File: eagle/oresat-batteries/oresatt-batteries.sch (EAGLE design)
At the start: 22 parts, among them U1 TCAN330

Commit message: Finished first draft of schematics.
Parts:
- removed Y1: (no value), low-gain-radio:CRYSTAL2.5X2.0MM
- added C10, C11, C12, C13: 100n, rcl:C-EUC0603
- added C8, C9: 20p, rcl:C-EUC0603
- added CF2: 2MM-RA-1X8, oresat-batteries:2MM-RA-1X8
- added D2: BAS40, diode:BAS40
- added R10, R12: 10k, rcl:R-US_R0603
- added R11, R7: (no value), rcl:R-US_R0603
- added R13: DNP/0, rcl:R-US_R0603
- added R8, R9: 4.7k, rcl:R-US_R0603
- added U$10, U$11, U$15, U$6, U$7, U$9: TP, oresat-batteries:TP
- added U2: STM32F042K6, oresat-batteries:STM32F042K6
- added X1: 16MHz, low-gain-radio:CRYSTAL-WITH-GND
- R1: value Sense -> THERMISTER
- R3: value Sense -> .01-.05
- R4: value Sense -> 200k .1%
- U$4: value STM32F042G -> TP; device oresat-batteries:STM32F042G -> oresat-batteries:TP
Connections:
- net N$1 renamed ADP_THR
- net N$10 renamed BQVMIN
- net N$2 renamed LEDNP
- net N$3 renamed ADP_LED
- net N$9 renamed STC_VIN
- removed net N$5: C5.1, CF1.3, U$1.VIN
- removed net N$6: C4.1
- removed net N$8: R3.2
- new net ADP_CBP: C4.1, U$1.CBP
- new net BQBAT: C1.1, R7.1, U$2.BAT
- new net CAN_EN: U1.SHDN, U2.PA10
- new net CAN_LSTN: U1.S, U2.PA9
- new net CAN_RX: U1.RXD, U2.PA11
- new net CAN_TX: U1.TXD, U2.PA12
- new net ISO_S: C3.1, CF1.2, U$1.ISO_S
- new net N$1: C7.2, R11.1, U$5.VCC
- new net N$2: R12.2, U2.PB8-BOOT0
- new net N$3: R10.1, R13.2, U$5.IO0
- new net N$31: CF2.3, U2.NRST
- new net OSC_IN: C8.1, U2.PF0-OSC_IN, X1.1
- new net OSC_OUT: C9.1, U2.PF1-OSC_OUT, X1.2
- new net SCL: R8.1, U$1.SCL, U$5.SCL, U2.PB6
- new net SDA: R9.1, U$1.SDA, U$5.SDA, U2.PB7
- new net STC_CG: R3.2, U$5.CG
- new net STC_IO: R13.1, U2.PB5
- new net STM_DEBUG: CF2.8, U2.PA4
- new net SWCLK: CF2.4, U2.PA14-SWCLK
- new net SWDIO: CF2.5, U2.PA13-SWDIO
- new net USART2_RX: CF2.7, U2.PA3
- new net USART2_TX: CF2.6, U2.PA2
- new net VSOLAR: C5.1, CF1.3, R8.2, R9.2, U$1.VIN
- net GND: now also C10.2, C11.2, C12.2, C13.2, C8.2, C9.2, CF2.1, R12.1, U1.GND, U2.VSS, X1.SHIELD
- net N$4: now also D2.C; no longer C3.1, U$1.ISO_S
- net VBAT+: now also C10.1, C11.1, C12.1, C13.1, CF2.2, D2.A, R11.2, R7.2, U1.VCC, U2.VDD, U2.VDDA, U2.VDDIO2; no longer C1.1, C7.2, U$2.BAT, U$5.VCC
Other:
- note added: "CAN_EN"
- note added: "CAN_LSTN"
- note added: "CAN_RX"
- note added: "CAN_TX"
- note added: "DEBUG"
- note added: "DO I WANT TO SHUTDOWN?"
- note added: "MISSING: Resistive heater Full SHUTDOWN"
- note added: "RESET"
- note added: "SCL"
- note added: "SDA"
- note added: "SWCLK"
- note added: "SWDIO"
- note added: "USART2_RX"
- note added: "USART2_TX"
- note added: "VBATT+"
- note added: "VSOLAR"
- note added: "WE NEED A PLACE TO CHAT"
- note added: "WE NEED FETS! 20 AMPS MAX DISCHARGE"
- moved on the sheet: C1, C2, C3, C4, C5, C6, C7, CF1, LED1, R1, R2, R3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

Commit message: Minor clean up, added debug board, serial marker
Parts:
- added DEBUG_DNP: (no value), pinhead:PINHD-2X8
- added U$12, U$16, U$17, U$8: TP, oresat-batteries:TP
- added U$13, U$14: CSD16340Q3, oresat-batteries:CSD16340Q3
- R8, R9: value 4.7k -> 1.6k
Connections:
- removed net VBAT+: C10.1, C11.1, C12.1, C13.1, C2.1, CF2.2, D2.A, R11.2, R5.1, R7.2, U$1.BAT_SNS, U$1.ISO_B, U1.VCC, U2.VDD, U2.VDDA, U2.VDDIO2
- new net N$10: U$14.G, U$2.DOUT
- new net N$11: U$13.G, U$2.COUT
- new net N$5: CF1.4, DEBUG_DNP.13, DEBUG_DNP.14, U1.CANH
- new net N$6: CF1.5, DEBUG_DNP.11, DEBUG_DNP.12, U1.CANL
- new net N$9: U$13.D, U$14.D
- new net VBATT+: C10.1, C11.1, C12.1, C13.1, C2.1, CF2.2, D2.A, DEBUG_DNP.1, DEBUG_DNP.2, R11.2, R5.1, R7.2, R8.2, R9.2, U$1.BAT_SNS, U$1.ISO_B, U1.VCC, U2.VDD, U2.VDDA, U2.VDDIO2
- net GND: now also DEBUG_DNP.15, DEBUG_DNP.16, U$13.S
- net SCL: now also R9.1; no longer R8.1
- net SDA: now also R8.1; no longer R9.1
- net STC_CG: now also U$14.S
- net USART2_RX: now also DEBUG_DNP.5, DEBUG_DNP.6
- net USART2_TX: now also DEBUG_DNP.3, DEBUG_DNP.4
- net VSOLAR: now also DEBUG_DNP.7, DEBUG_DNP.8; no longer R8.2, R9.2
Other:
- note added: "CANH"
- note added: "CANL"
- note added: "GND"
- note added: "High Side Battery shut-off"
- note added: "Low side shut-off NANOracks req"
- note added: "MISSING: Resistive heater Full SHUTDOWN Two high one low complete crowbar"
- note added: "UARTRX"
- note added: "UARTX"
- note added: "add ground pin clips NP"
- note added: "add pins"
- note removed: "MISSING: Resistive heater Full SHUTDOWN"
- note removed: "WE NEED A PLACE TO CHAT"
- note removed: "WE NEED FETS! 20 AMPS MAX DISCHARGE"
- moved on the sheet: C1, C2, C3, C4, C5, CF1, D2, LED1, R1, R2, R5, R6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

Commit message: Added, resistive heater, half of shutdown circuitry, connected DIG_IOx and SYS_EN pins.
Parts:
- added R14: 100k, rcl:R-US_R0603
- added U$18, U$19, U$20: CSD16340Q3, oresat-batteries:CSD16340Q3
- added U$21: 4.19, oresat-batteries:RES_HEATER
- U$3: value 1.5AHBATT -> 2AHBATT; device oresat-batteries:1.5AHBATT -> oresat-batteries:2AHBATT
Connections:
- net N$11 renamed COUT
- net N$9 renamed BETSHUT
- new net BATTHICUT: U$19.D, U$3.V+
- new net BQKILL: R6.2, U$18.D, U$2.VSS
- new net DOUT: CF1.40, R14.1, U$14.G, U$18.G, U$19.G, U$2.DOUT
- new net N$11: U$1.DIG_IO3, U2.PB4
- new net N$13: U$20.S, U$21.1
- new net N$14: U$20.G, U2.PA1
- new net N$8: U$1.SYS_EN, U2.PB0
- new net N$9: U$1.DIG_IO1, U2.PB1
- net GND: now also U$18.S, U$21.2; no longer R6.2, U$2.VSS
- net N$10: now also U$1.DIG_IO2, U2.PB3; no longer U$14.G, U$2.DOUT
- net STC_CG: now also U$3.V-
- net STC_VIN: now also R5.1; no longer R5.2
- net VBATT+: now also R14.2, R5.2, U$19.S, U$20.D; no longer R5.1
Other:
- note added: "DIG_IO1"
- note added: "DIG_IO2"
- note added: "DIG_IO3"
- note added: "HEAT"
- note added: "SHORT_BAR"
- note added: "SYS_EN"
- note added: "This won't work"
- note added: "VBATTSUPP"
- note removed: "High Side Battery shut-off"
- note removed: "Low side shut-off NANOracks req"
- moved on the sheet: C1, C10, C11, C12, C13, C2, C4, C6, CF2, DEBUG_DNP, R12, R5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

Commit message: Fixed Shutdown Circuit, Added more ground pins, cleaned up schematic
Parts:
- added R15: 100k, rcl:R-US_R0603
- added U$22, U$23: TP, oresat-batteries:TP
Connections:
- new net SHORTBAR: CF1.40, R14.1, R15.1, U$18.G, U$19.G
- net DOUT: no longer CF1.40, R14.1, U$18.G, U$19.G
- net GND: now also R15.2
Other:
- note added: "ISO_Sx"
- note removed: "DO I WANT TO SHUTDOWN?"
- note removed: "MISSING: Resistive heater Full SHUTDOWN Two high one low complete crowbar"
- note removed: "This won't work"
- moved on the sheet: D2, U$16, U$17, U$18

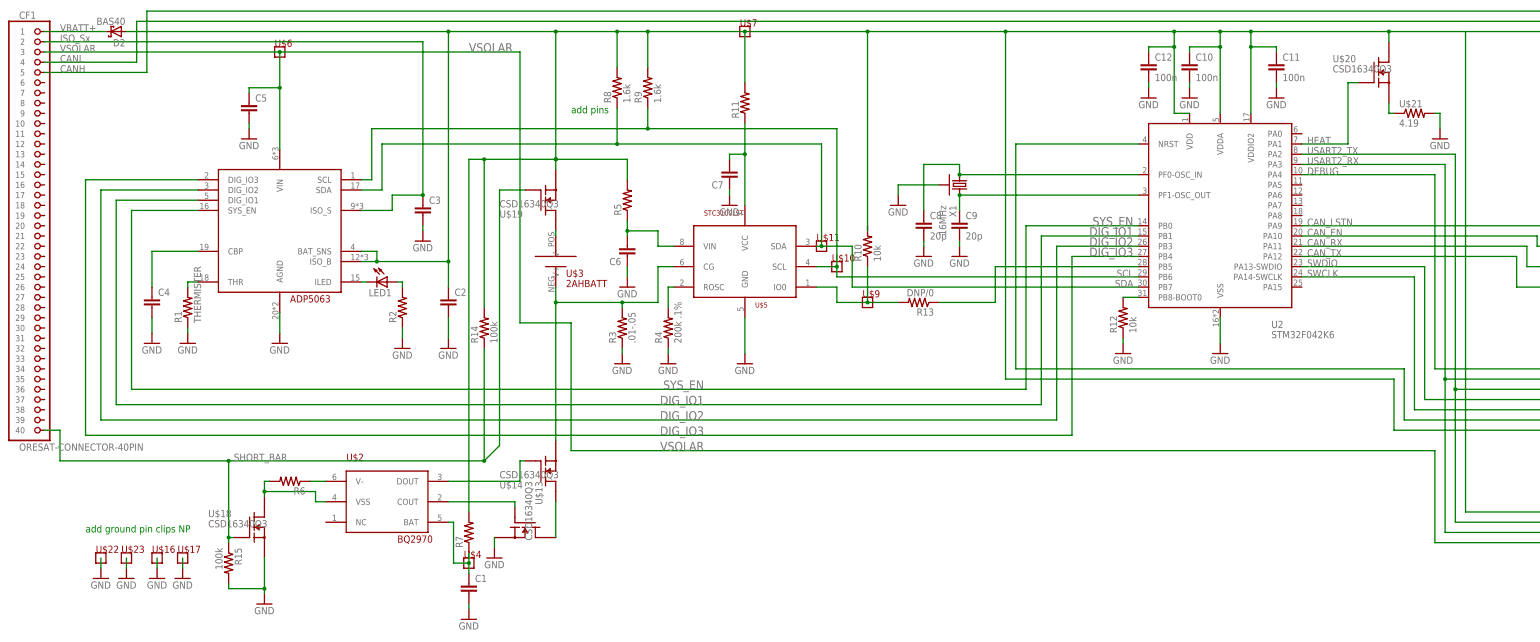
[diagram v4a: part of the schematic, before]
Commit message: Added TP and nominal V for shutoff
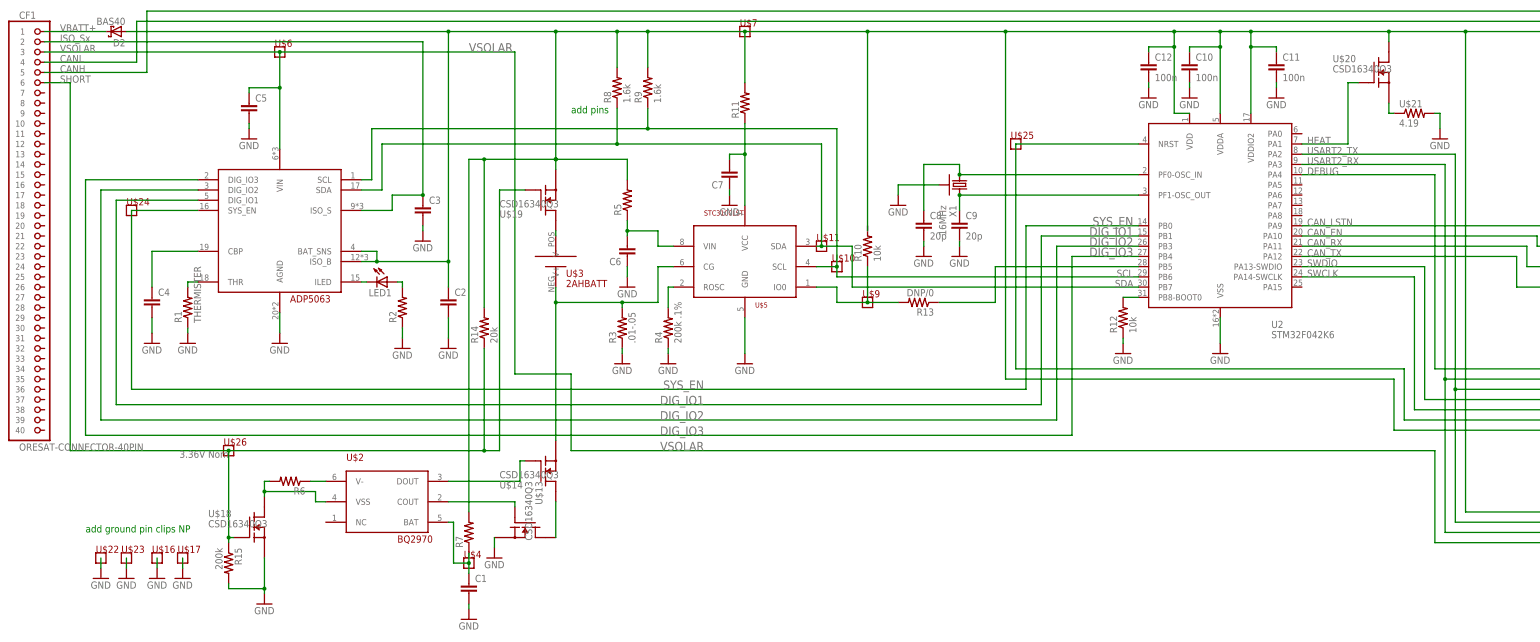
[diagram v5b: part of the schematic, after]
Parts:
- added U$24, U$25, U$26: TP, oresat-batteries:TP
- R14: value 100k -> 20k
- R15: value 100k -> 200k
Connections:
- net SHORTBAR: now also CF1.6; no longer CF1.40
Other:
- note added: "3.36V Nom"
- note added: "SHORT"
- note removed: "SHORT_BAR"

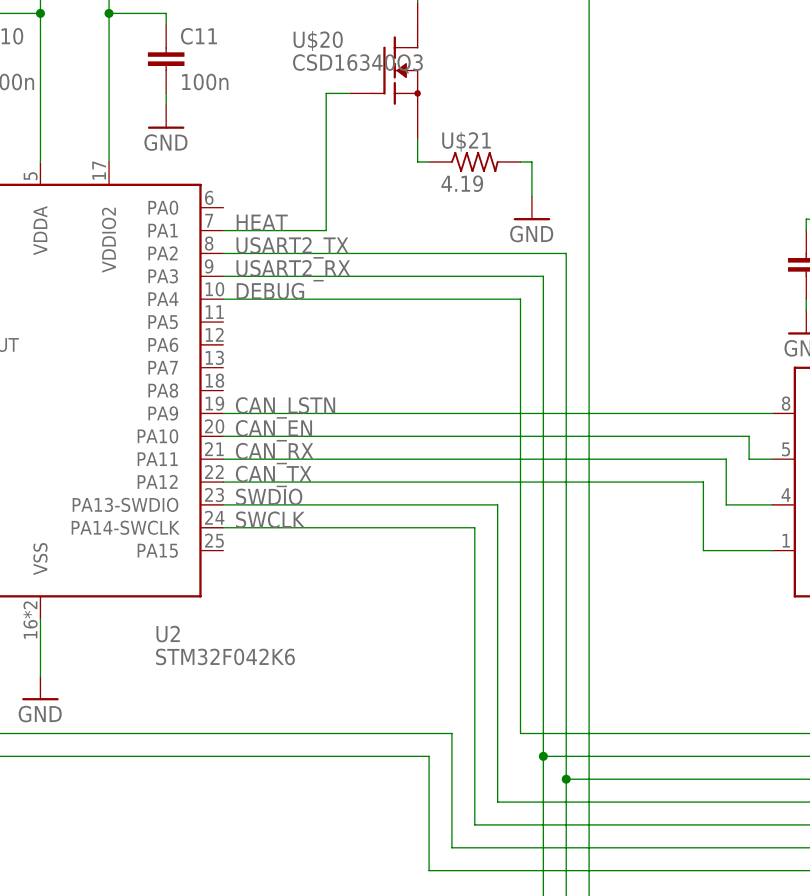
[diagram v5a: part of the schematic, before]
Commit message: Named missing NETS
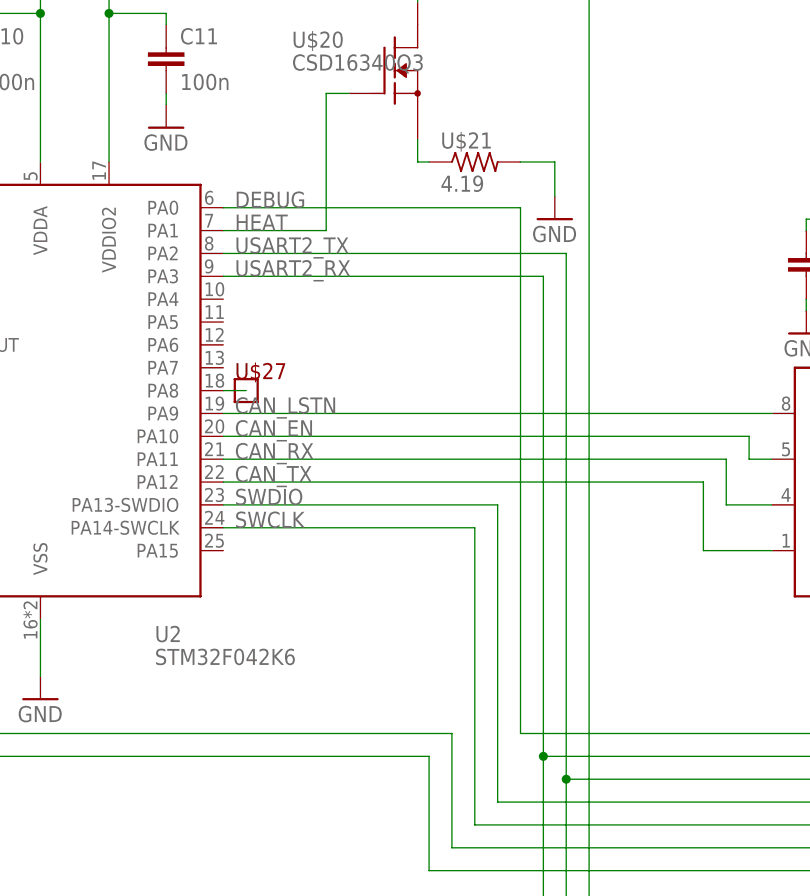
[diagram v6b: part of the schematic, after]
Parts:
- added U$27: TP, oresat-batteries:TP
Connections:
- net N$10 renamed DIG_IO2
- net N$11 renamed DIG_IO3
- net N$14 renamed HEAT
- net N$3 renamed IO0
- net N$31 renamed NRESET
- net N$5 renamed CANH
- net N$6 renamed CANL
- net N$7 renamed ROSC
- net N$8 renamed SYS_EN
- net N$9 renamed DIG_IO1
- new net PA8: U2.PA8
- net STM_DEBUG: now also U2.PA0; no longer U2.PA4
